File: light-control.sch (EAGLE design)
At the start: 28 parts, among them IC1 ULN2003AN, IC2 MEGA8-P, K1 JS-M1-12V-5, K2 JS-M1-12V-5, K3 JS-M1-12V-5, K4 JS-M1-12V-5

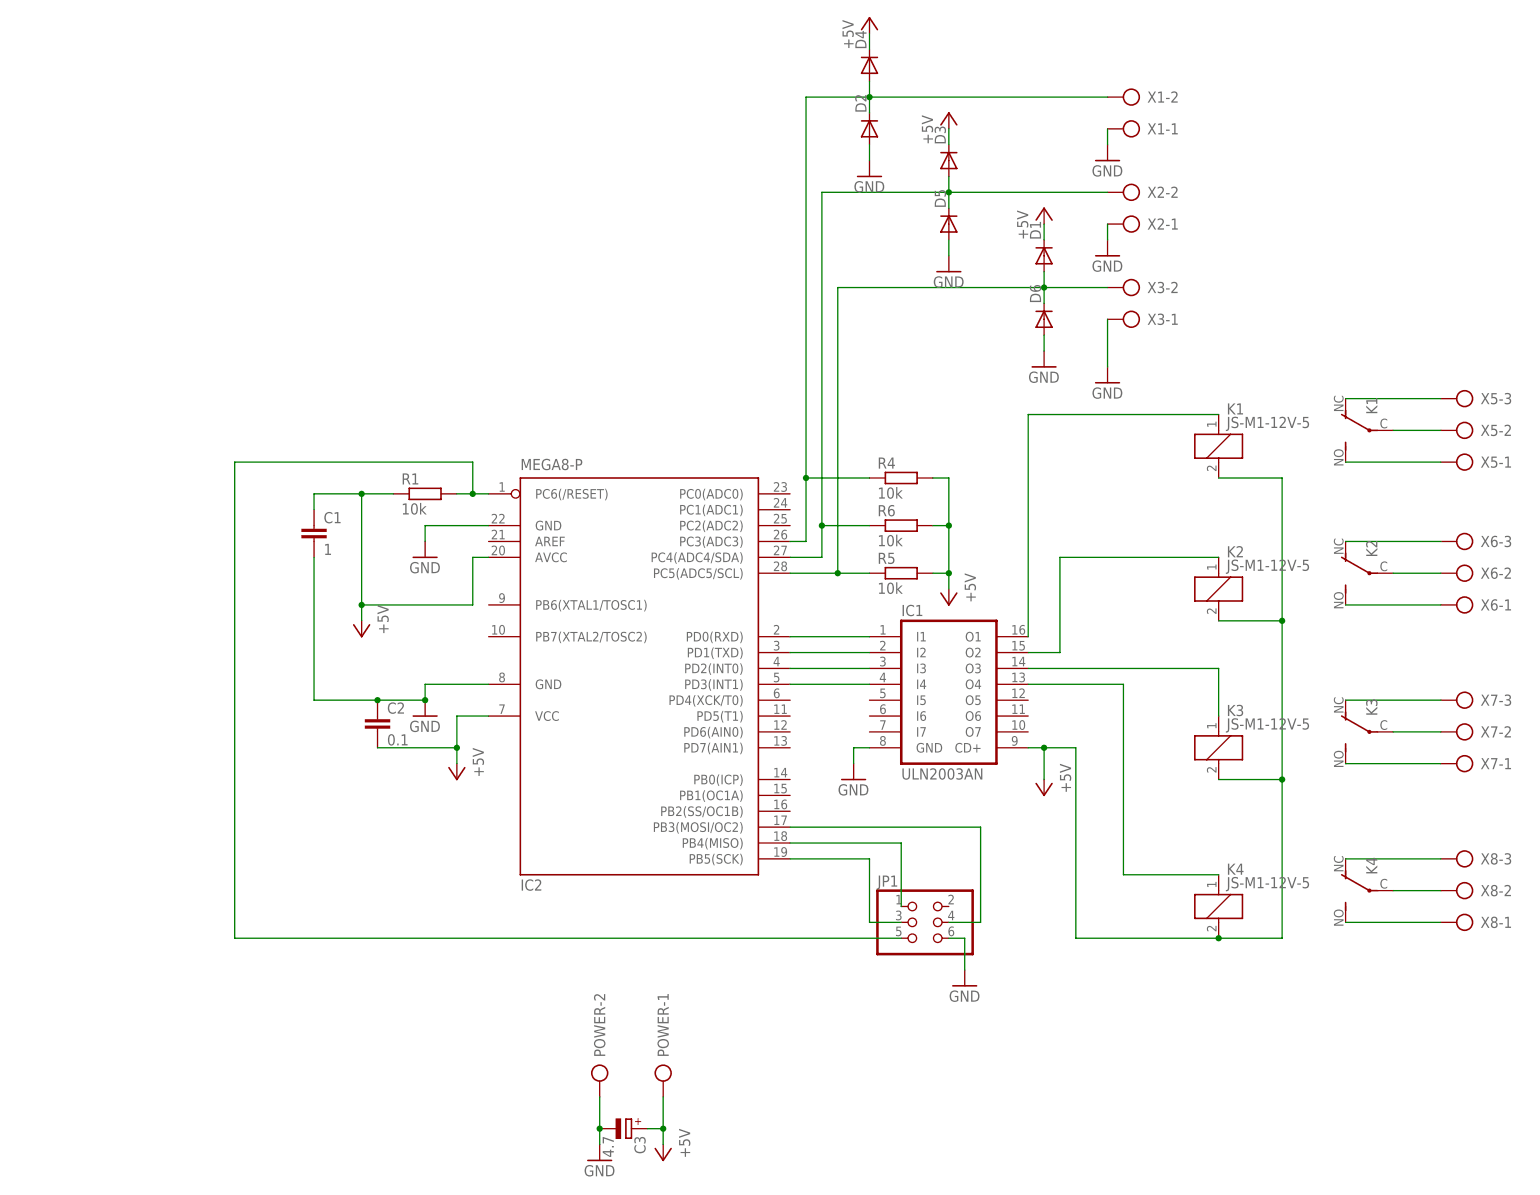
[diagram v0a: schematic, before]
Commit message: Moved to TQFP
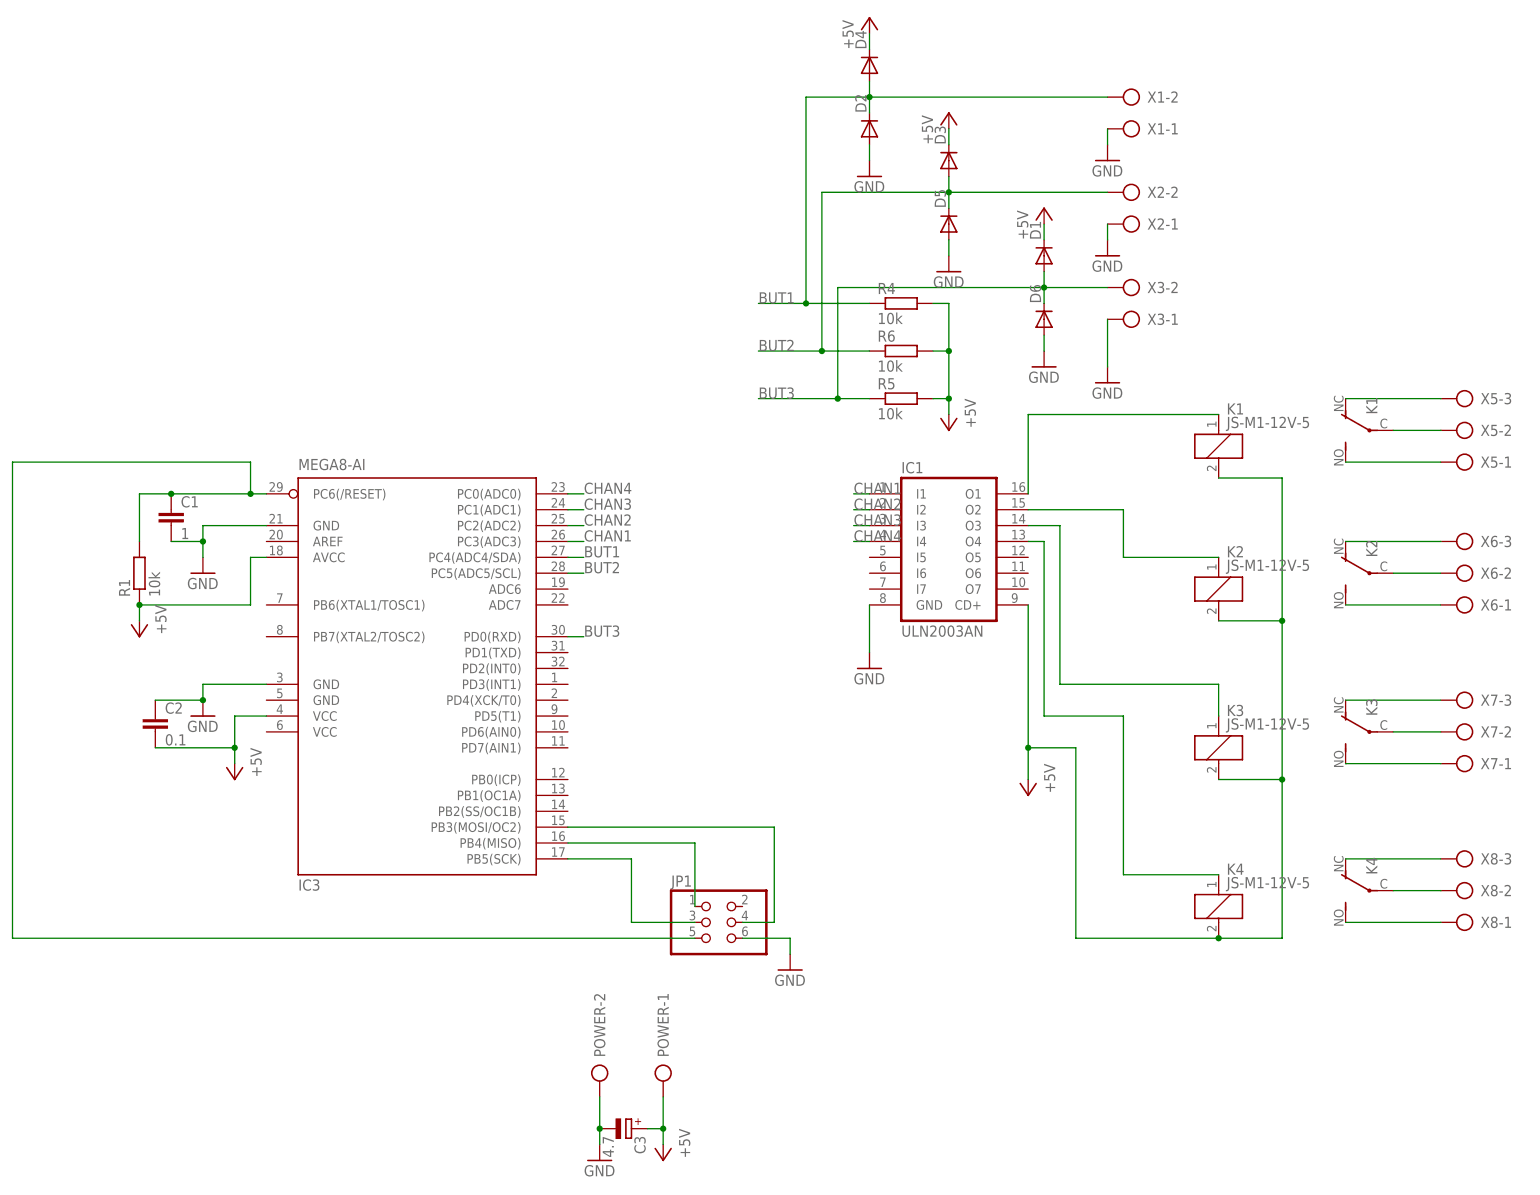
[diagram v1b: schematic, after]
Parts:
- removed IC2: MEGA8-P, atmel:MEGA8-P
- added IC3: MEGA8-AI, atmel:MEGA8-AI
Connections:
- removed net N$1: IC1.I1, IC2.PD0(RXD)
- removed net N$21: D2.C, D4.A, IC2.PC3(ADC3), R4.1, X1-2.KL
- removed net N$22: D3.A, D5.C, IC2.PC4(ADC4/SDA), R6.1, X2-2.KL
- removed net N$23: D1.A, D6.C, IC2.PC5(ADC5/SCL), R5.1, X3-2.KL
- removed net N$6: IC1.I2, IC2.PD1(TXD)
- removed net N$7: IC1.I3, IC2.PD2(INT0)
- removed net N$8: IC1.I4, IC2.PD3(INT1)
- new net BUT1: D2.C, D4.A, IC3.PC4(ADC4/SDA), R4.1, X1-2.KL
- new net BUT2: D3.A, D5.C, IC3.PC5(ADC5/SCL), R6.1, X2-2.KL
- new net BUT3: D1.A, D6.C, IC3.PD0(RXD), R5.1, X3-2.KL
- new net CHAN1: IC1.I1, IC3.PC3(ADC3)
- new net CHAN2: IC1.I2, IC3.PC2(ADC2)
- new net CHAN3: IC1.I3, IC3.PC1(ADC1)
- new net CHAN4: IC1.I4, IC3.PC0(ADC0)
- net +5V: now also IC3.AVCC, IC3.VCC@1; no longer C1.1, IC2.AVCC, IC2.VCC@1
- net GND: now also IC3.GND, IC3.GND@1; no longer IC2.GND, IC2.GND@1
- net N$2: now also IC3.PB4(MISO); no longer IC2.PB4(MISO)
- net N$3: now also IC3.PB5(SCK); no longer IC2.PB5(SCK)
- net N$4: now also IC3.PB3(MOSI/OC2); no longer IC2.PB3(MOSI/OC2)
- net N$5: now also C1.1, IC3.PC6(/RESET); no longer IC2.PC6(/RESET)
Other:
- moved on the sheet: C1, C2, IC1, JP1, R1, R4, R5, R6

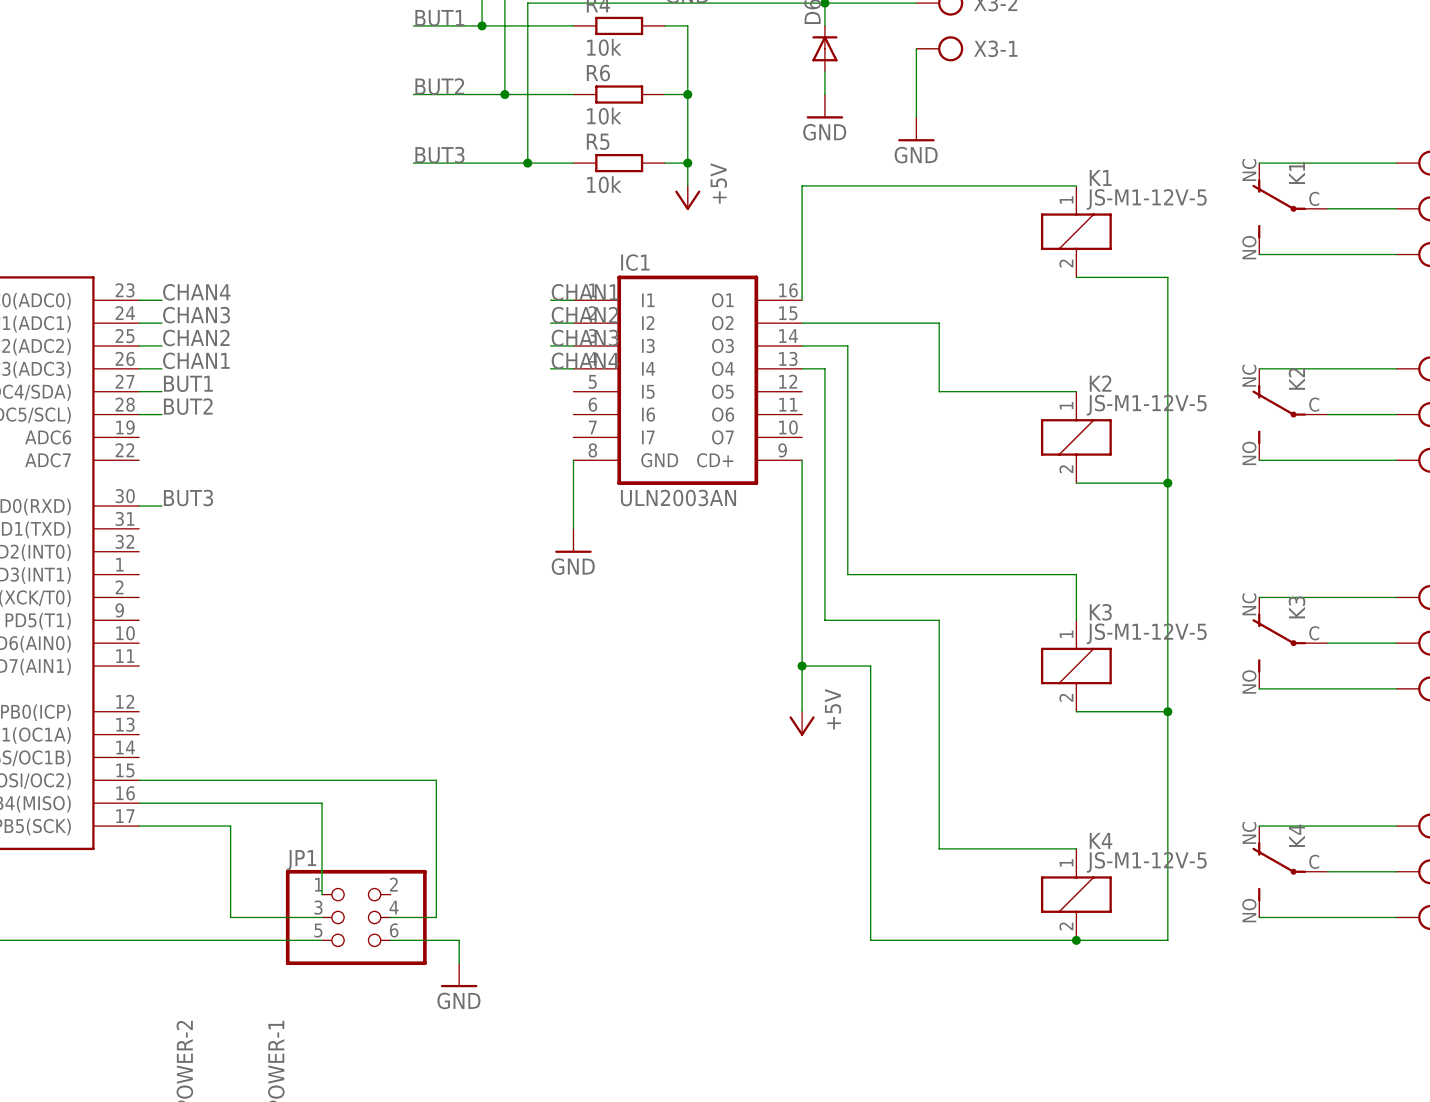
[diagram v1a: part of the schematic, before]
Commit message: Fixed schematic
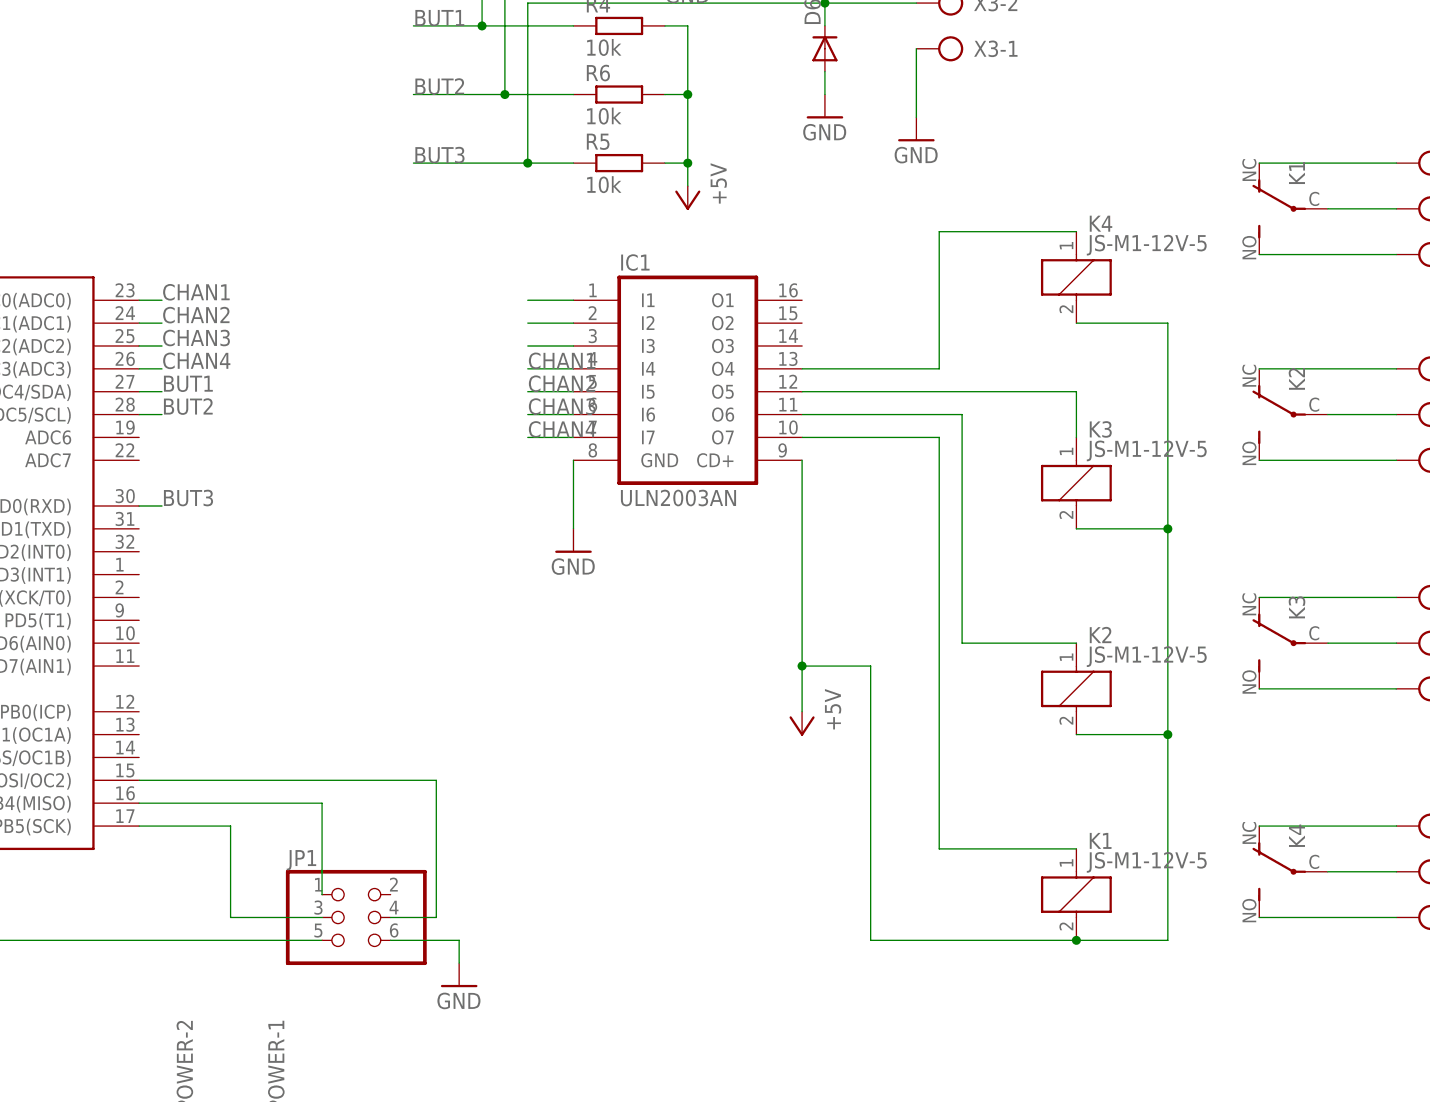
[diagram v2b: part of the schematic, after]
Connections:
- removed net N$12 (its old number): IC1.O3, K31.1
- new net N$1: IC1.I1
- new net N$6: IC1.I2
- new net N$7: IC1.I3
- new net N$8: IC1.O7, K11.1
- net CHAN1: now also IC1.I4, IC3.PC0(ADC0); no longer IC1.I1, IC3.PC3(ADC3)
- net CHAN2: now also IC1.I5, IC3.PC1(ADC1); no longer IC1.I2, IC3.PC2(ADC2)
- net CHAN3: now also IC1.I6, IC3.PC2(ADC2); no longer IC1.I3, IC3.PC1(ADC1)
- net CHAN4: now also IC1.I7, IC3.PC3(ADC3); no longer IC1.I4, IC3.PC0(ADC0)
- net N$10: now also IC1.O6, K21.1; no longer IC1.O1, K11.1
- net N$11: now also IC1.O5, K31.1; no longer IC1.O2, K21.1
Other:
- moved on the sheet: K1, K2, K3, K4
